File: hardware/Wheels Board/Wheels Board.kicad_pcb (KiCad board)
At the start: 2 copper layers, 92.9 x 69.7 mm, 46 parts, among them J1 Conn_01x05, J10 gnd, J11 hall_out, J12 Conn_01x05, J2 24v, J3 Conn_01x03, J4 53307-2471, J6 Conn_01x05_Pin, J7 Conn_01x07, J8 24v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

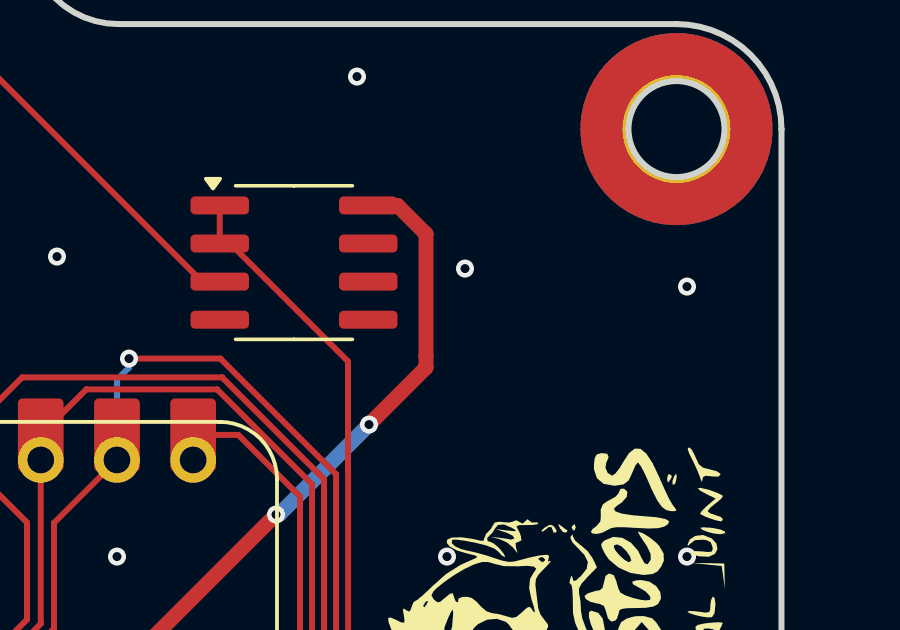
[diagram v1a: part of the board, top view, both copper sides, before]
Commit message: added bypass cap to hall
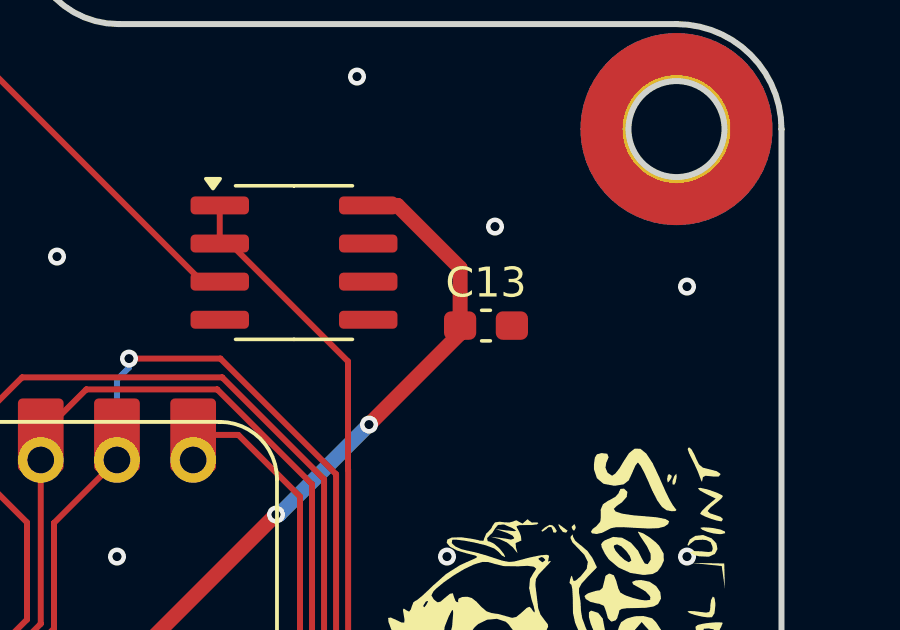
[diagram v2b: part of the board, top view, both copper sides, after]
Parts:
- added C13: 1uf, Capacitor_SMD:C_0603_1608Metric_Pad1.08x0.95mm_HandSolder, F.Cu at (136.3, 62.3)
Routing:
- net +3.3V: track 76.2 -> 77.1 mm

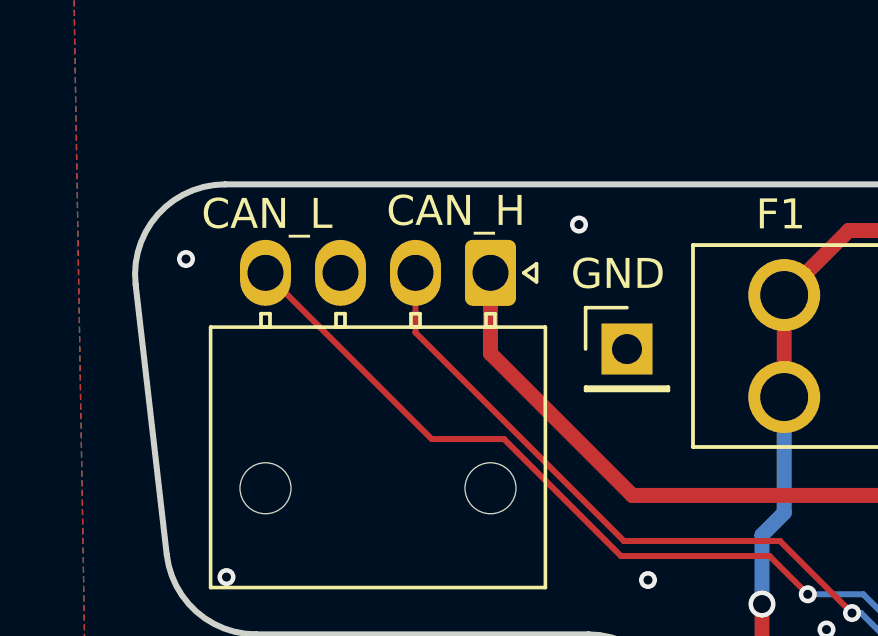
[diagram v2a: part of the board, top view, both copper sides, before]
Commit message: changed hall conn, silkscreen fix
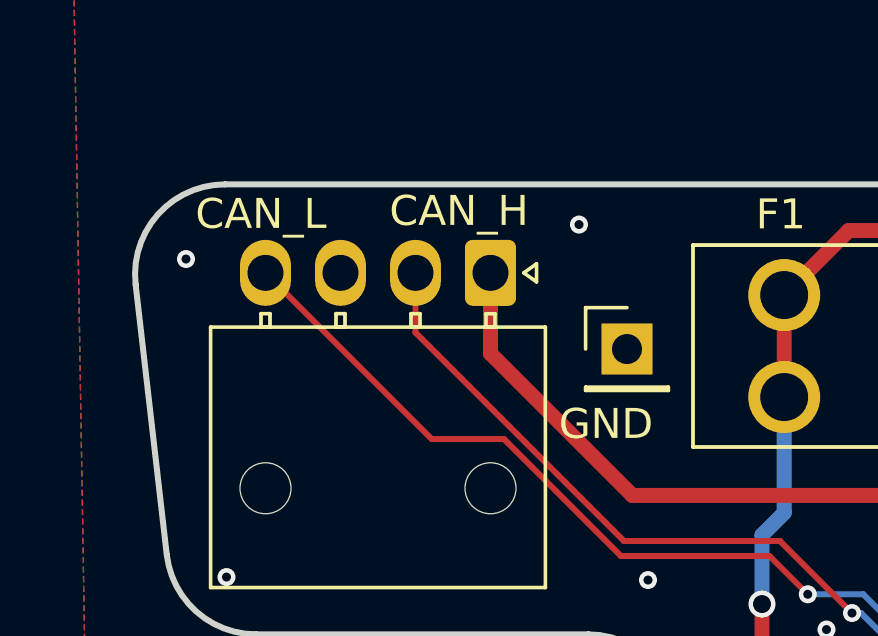
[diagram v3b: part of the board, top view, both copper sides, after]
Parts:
- removed LOGO1: LHRS, UTSVT_Logos:LHRs_LOGO
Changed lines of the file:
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@@
 		)
 	)
-	(footprint "UTSVT_Logos:LHRs_LOGO"
-		(layer "F.Cu")
-		(at 44.085562 152.70907)
-		(property "Reference" "LOGO1"
-			(at 2.286 8.128 0)
-			(layer "F.SilkS")
-			(hide yes)
-			(effects
-				(font
-					(size 1.5 1.5)
-					(thickness 0.3)
-				)
-			)
-		)
-		(property "Value" "LHRS"
-			(at 0.75 0 0)
-			(layer "F.SilkS")
-			(hide yes)
-			(effects
-				(font
-					(size 1.5 1.5)
-					(thickness 0.3)
-				)
-			)
-		)
-		(property "Datasheet" ""
-			(at 0 0 0)
-			(layer "F.Fab")
-			(hide yes)
-			(effects
-				(font
-					(size 1.27 1.27)
-					(thickness 0.15)
-				)
-			)
-		)
-		(property "Description" "Graph footprint placeholder"
-			(at 0 0 0)
-			(layer "F.Fab")
-			(hide yes)
-			(effects
-				(font
-					(size 1.27 1.27)
-					(thickness 0.15)
-				)
-			)
-		)
-		(property "PN" ""
-			(at 0 0 0)
-			(unlocked yes)
-			(layer "F.Fab")
-			(hide yes)
-			(effects
-				(font
-					(size 1 1)
-					(thickness 0.15)
-				)
-			)
-		)
-		(property "p/n" ""
-			(at 0 0 0)
-			(unlocked yes)
-			(layer "F.Fab")
-			(hide yes)
-			(effects
-				(font
-					(size 1 1)
-					(thickness 0.15)
-				)
-			)
-		)
-		(property "Id" ""
-			(at 0 0 0)
-			(unlocked yes)
-			(layer "F.Fab")
-			(hide yes)
-			(effects
-				(font
-					(size 1 1)
-					(thickness 0.15)
-				)
-			)
-		)
-		(property "MAXIMUM_PACKAGE_HEIGHT" ""
-			(at 0 0 0)
-			(unlocked yes)
-			(layer "F.Fab")
-			(hide yes)
-			(effects
-				(font
-					(size 1 1)
-					(thickness 0.15)
-				)
-			)
-		)
-		(property "PARTREV" ""
-			(at 0 0 0)
-			(unlocked yes)
-			(layer "F.Fab")
-			(hide yes)
-			(effects
-				(font
-					(size 1 1)
-					(thickness 0.15)
-				)
-			)
-		)
-		(property "STANDARD" ""
-			(at 0 0 0)
-			(unlocked yes)
-			(layer "F.Fab")
-			(hide yes)
-			(effects
-				(font
-					(size 1 1)
-					(thickness 0.15)
-				)
-			)
-		)
-		(property "Vds" ""
-			(at 0 0 0)
-			(unlocked yes)
-			(layer "F.Fab")
-			(hide yes)
-			(effects
-				(font
-					(size 1 1)
-					(thickness 0.15)
-				)
-			)
-		)
-		(sheetname "/")
-		(sheetfile "Wheels Board.kicad_sch")
-		(attr board_only exclude_from_pos_files)
-		(fp_poly
-			(pts
-				(xy -6.249206 -0.203095) (xy -6.224007 0.930833) (xy -5.203472 0.944476) (xy -4.182936 0.958119)
-				(xy -4.182936 1.209059) (xy -4.182936 1.46) (xy -5.519249 1.46) (xy -6.855562 1.46) (xy -6.842166 0.061488)
-				(xy -6.828769 -1.337024) (xy -6.551587 -1.337024) (xy -6.274404 -1.337024)
-			)
-			(stroke
-				(width 0)
-				(type solid)
-			)
-			(fill yes)
-			(layer "F.Mask")
-		)
-		(fp_poly
-			(pts
-				(xy 6.615873 -0.689802) (xy 6.615873 -0.463016) (xy 5.834722 -0.463016) (xy 5.053571 -0.463016)
-				(xy 5.053571 -0.211032) (xy 5.053571 0.040952) (xy 5.834722 0.040952) (xy 6.615873 0.040952) (xy 6.615873 0.746508)
-				(xy 6.615873 1.452063) (xy 5.607936 1.452063) (xy 4.6 1.452063) (xy 4.6 1.225278) (xy 4.6 0.998492)
-				(xy 5.381151 0.998492) (xy 6.162301 0.998492) (xy 6.162301 0.746508) (xy 6.162301 0.494524) (xy 5.381151 0.494524)
-				(xy 4.6 0.494524) (xy 4.6 -0.211032) (xy 4.6 -0.916587) (xy 5.607936 -0.916587) (xy 6.615873 -0.916587)
-			)
-			(stroke
-				(width 0)
-				(type solid)
-			)
-			(fill yes)
-			(layer "F.Mask")
-		)
-		(fp_poly
-			(pts
-				(xy -0.373172 -1.35313) (xy -0.176388 -1.337024) (xy -0.162992 0.061488) (xy -0.149596 1.46) (xy -0.476322 1.46)
-				(xy -0.803048 1.46) (xy -0.817297 0.893036) (xy -0.831547 0.326071) (xy -1.926018 0.312494) (xy -3.02049 0.298916)
-				(xy -3.034749 0.866859) (xy -3.049007 1.434801) (xy -3.364789 1.449826) (xy -3.680571 1.464851)
-				(xy -3.66717 0.063914) (xy -3.653769 -1.337024) (xy -3.397309 -1.351975) (xy -3.19821 -1.347139)
-				(xy -3.089637 -1.30458) (xy -3.084272 -1.298756) (xy -3.058725 -1.221427) (xy -3.035949 -1.068757)
-				(xy -3.019124 -0.866199) (xy -3.013153 -0.729439) (xy -2.998611 -0.228294) (xy -1.915079 -0.228294)
-				(xy -0.831547 -0.228294) (xy -0.817248 -0.769526) (xy -0.807939 -1.027445) (xy -0.788229 -1.200221)
-				(xy -0.746219 -1.303491) (xy -0.67001 -1.352895) (xy -0.547702 -1.36407)
-			)
-			(stroke
-				(width 0)
-				(type solid)
-			)
-			(fill yes)
-			(layer "F.Mask")
-		)
-		(fp_poly
-			(pts
-				(xy 1.856389 -1.35712) (xy 2.179517 -1.353276) (xy 2.647725 -1.344807) (xy 3.025655 -1.332131) (xy 3.323823 -1.311144)
-				(xy 3.552744 -1.277743) (xy 3.722934 -1.227822) (xy 3.844908 -1.157279) (xy 3.929182 -1.062008)
-				(xy 3.986272 -0.937906) (xy 4.026693 -0.780868) (xy 4.055352 -0.621144) (xy 4.065781 -0.418686)
-				(xy 4.042188 -0.196195) (xy 3.991695 0.012348) (xy 3.921422 0.172966) (xy 3.877371 0.22816) (xy 3.81313 0.294076)
-				(xy 3.813297 0.346382) (xy 3.880288 0.426572) (xy 3.889499 0.436385) (xy 3.945563 0.511351) (xy 3.98223 0.608775)
-				(xy 4.005316 0.753634) (xy 4.020634 0.970905) (xy 4.022438 1.007429) (xy 4.044076 1.46) (xy 3.710332 1.46)
-				(xy 3.376588 1.46) (xy 3.376588 1.164415) (xy 3.364342 0.957713) (xy 3.321898 0.814351) (xy 3.272136 0.736042)
-				(xy 3.167685 0.603254) (xy 2.213803 0.603254) (xy 1.259921 0.603254) (xy 1.259921 1.031627) (xy 1.259921 1.46)
-				(xy 0.932342 1.46) (xy 0.604762 1.46) (xy 0.604762 0.075047) (xy 0.604762 -0.387884) (xy 1.259921 -0.387884)
-				(xy 1.264188 -0.190347) (xy 1.275542 -0.032626) (xy 1.291816 0.059012) (xy 1.297719 0.070099) (xy 1.357819 0.081199)
-				(xy 1.502244 0.089204) (xy 1.714564 0.093761) (xy 1.978345 0.094519) (xy 2.277158 0.091126) (xy 2.278719 0.091098)
-				(xy 2.615482 0.084007) (xy 2.865965 0.07561) (xy 3.044681 0.064404) (xy 3.166141 0.048885) (xy 3.244859 0.027551)
-				(xy 3.295349 -0.001103) (xy 3.311853 -0.015907) (xy 3.377195 -0.134038) (xy 3.401407 -0.325503)
-				(xy 3.401786 -0.360538) (xy 3.391791 -0.529871) (xy 3.35341 -0.636804) (xy 3.28281 -0.711516) (xy 3.23272 -0.745454)
-				(xy 3.168423 -0.770399) (xy 3.074814 -0.787713) (xy 2.936788 -0.798753) (xy 2.73924 -0.804877) (xy 2.467064 -0.807446)
-				(xy 2.211878 -0.807857) (xy 1.259921 -0.807857) (xy 1.259921 -0.387884) (xy 0.604762 -0.387884)
-				(xy 0.604762 -1.309905) (xy 0.730608 -1.341491) (xy 0.813764 -1.349274) (xy 0.982805 -1.35485) (xy 1.222847 -1.358097)
-				(xy 1.519004 -1.358894)
-			)
-			(stroke
-				(width 0)
-				(type solid)
-			)
-			(fill yes)
-			(layer "F.Mask")
-		)
-		(embedded_fonts no)
-	)
 	(footprint "Connector_PinHeader_2.54mm:PinHeader_1x01_P2.54mm_Vertical"
 		(layer "F.Cu")
@@
 		(sheetname "/")
 		(sheetfile "Wheels Board.kicad_sch")
-		(attr through_hole)
+		(attr through_hole exclude_from_pos_files)
 		(fp_line
 			(start -8 -3.365)
@@
 	)
 	(gr_text "GND\n"
-		(at 69.3 69.9 0)
+		(at 68.9 74.9 0)
 		(layer "F.SilkS")
 		(effects
@@
 	)
 	(gr_text "CAN_L"
-		(at 57.6 67.9 0)
+		(at 57.4 67.9 0)
 		(layer "F.SilkS")
 		(effects
@@
 	)
 	(gr_text "CAN_H\n"
-		(at 63.9 67.8 0)
+		(at 64 67.8 0)
 		(layer "F.SilkS")
 		(effects

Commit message: last changes in bom
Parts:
- J3: footprint Connector_PinHeader_2.54mm:PinHeader_1x03_P2.54mm_Horizontal -> UTSVT_Connectors:105313-1103
- moved J3 0.51 mm to (109.1, 47.8)
